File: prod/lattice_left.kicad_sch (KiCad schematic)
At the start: 84 parts, among them J1 USB_C_Receptacle, J2 USB_C_Receptacle, J3 Conn_01x05, SW1 SW_Push, SW2 SW_Push, U1 RP2040, U2 XC6206PxxxMR, U3 USBLC6-2SC6, U4 W25Q128JVS, Y1 12MHz

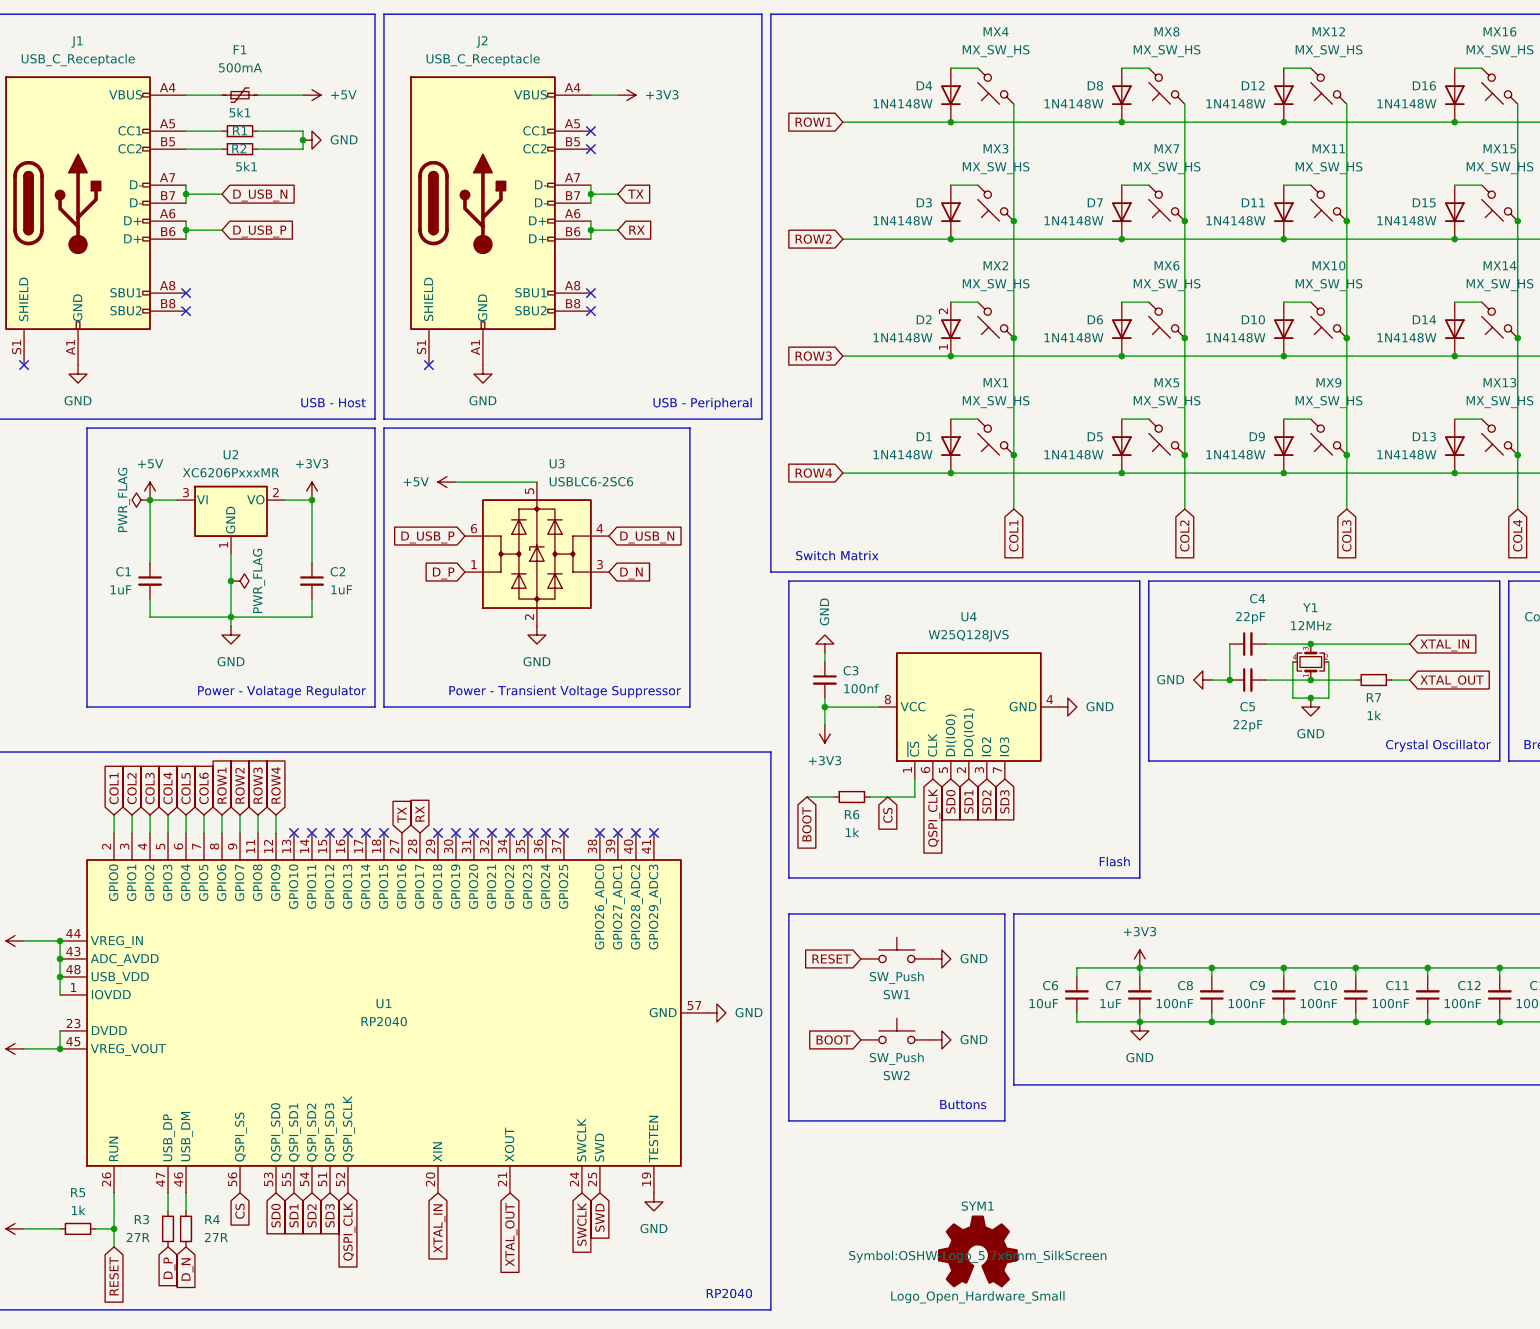
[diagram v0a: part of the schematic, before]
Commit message: component placement
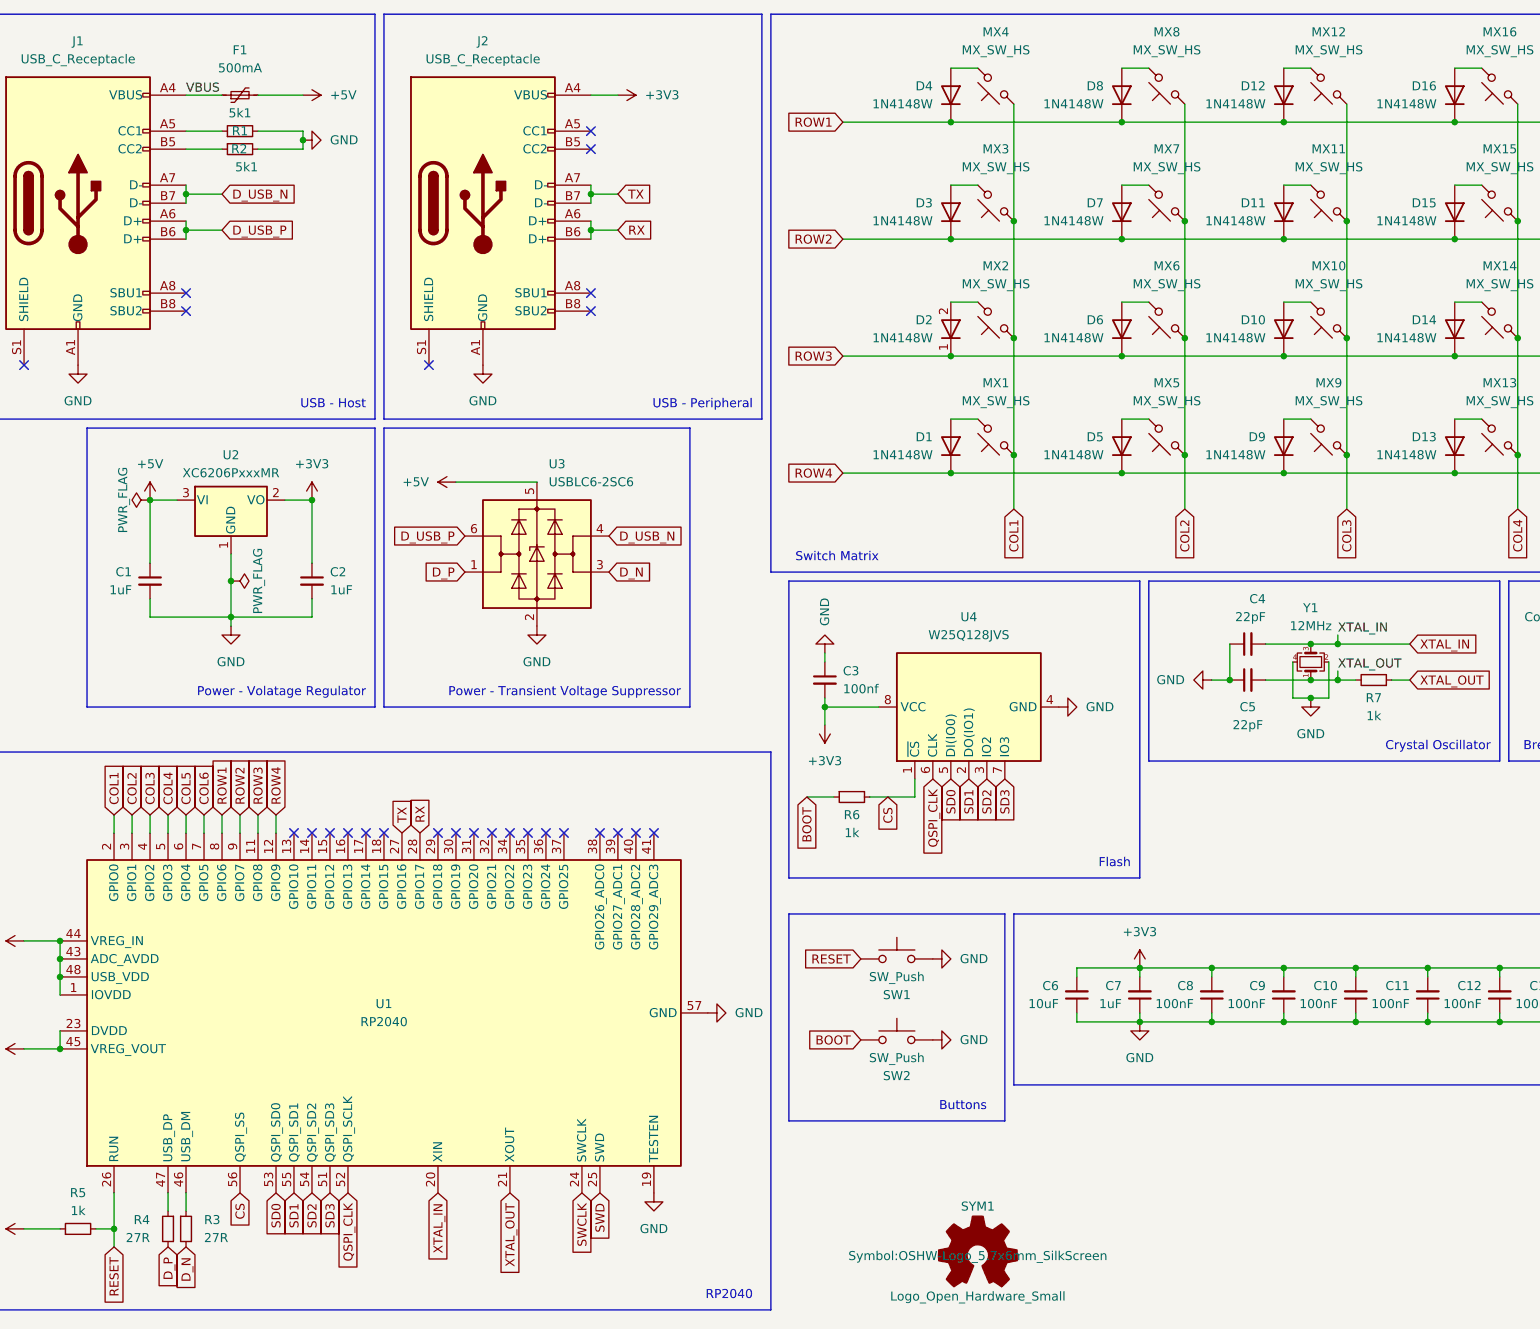
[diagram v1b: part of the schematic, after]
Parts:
- renumbered R4 to R3, R3 to R4
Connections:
- net XTAL_OUT: now also C5.2, R7.2, Y1.1
- net VBUS: now reaches F1.1, J1.A4 (VBUS), J1.A9 (VBUS), J1.B4 (VBUS), J1.B9 (VBUS)
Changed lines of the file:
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@@
   (junction (at 204.47 107.95) (diameter 0) (color 0 0 0 0)
   )
+  (junction (at 208.28 102.87) (diameter 0) (color 0 0 0 0)
+  )
   (junction (at 248.92 78.74) (diameter 0) (color 0 0 0 0)
   )
@@
   (junction (at 52.07 93.98) (diameter 0) (color 0 0 0 0)
   )
+  (junction (at 208.28 107.95) (diameter 0) (color 0 0 0 0)
+  )
   (junction (at 220.98 148.59) (diameter 0) (color 0 0 0 0)
   )
@@
     (stroke (width 0) (type default))
   )
+  (wire (pts (xy 208.28 101.6) (xy 208.28 102.87))
+    (stroke (width 0) (type default))
+  )
   (wire (pts (xy 186.69 26.67) (xy 186.69 43.18))
     (stroke (width 0) (type default))
@@
     (stroke (width 0) (type default))
   )
+  (wire (pts (xy 208.28 106.68) (xy 208.28 107.95))
+    (stroke (width 0) (type default))
+  )
   (wire (pts (xy 177.8 45.72) (xy 200.66 45.72))
     (stroke (width 0) (type default))
@@
     (stroke (width 0) (type default))
   )
-  (wire (pts (xy 204.47 107.95) (xy 210.82 107.95))
+  (wire (pts (xy 204.47 107.95) (xy 208.28 107.95))
     (stroke (width 0) (type default))
   )
@@
     (stroke (width 0) (type default))
   )
-  (wire (pts (xy 204.47 102.87) (xy 218.44 102.87))
+  (wire (pts (xy 204.47 102.87) (xy 208.28 102.87))
     (stroke (width 0) (type default))
   )
@@
     (stroke (width 0) (type default))
   )
+  (wire (pts (xy 208.28 102.87) (xy 218.44 102.87))
+    (stroke (width 0) (type default))
+  )
   (wire (pts (xy 241.3 148.59) (xy 241.3 149.86))
     (stroke (width 0) (type default))
@@
     (stroke (width 0) (type default))
   )
+  (wire (pts (xy 208.28 107.95) (xy 210.82 107.95))
+    (stroke (width 0) (type default))
+  )
   (wire (pts (xy 180.34 148.59) (xy 180.34 149.86))
     (stroke (width 0) (type default))
@@
     (effects (font (size 1.27 1.27)) (justify right bottom))
   )
+  (label "VBUS" (at 45.72 25.4 0) (fields_autoplaced)
+    (effects (font (size 1.27 1.27)) (justify left bottom))
+  )
+  (label "XTAL_IN" (at 208.28 101.6 0) (fields_autoplaced)
+    (effects (font (size 1.27 1.27)) (justify left bottom))
+  )
+  (label "XTAL_OUT" (at 208.28 106.68 0) (fields_autoplaced)
+    (effects (font (size 1.27 1.27)) (justify left bottom))
+  )
   (global_label "ROW1" (shape input) (at 138.43 29.21 180) (fields_autoplaced)
     (effects (font (size 1.27 1.27)) (justify right))
@@
     )
   )
-  (symbol (lib_id "Device:R_Small") (at 43.18 185.42 0) (unit 1)
-    (in_bom yes) (on_board yes) (dnp no) (fields_autoplaced)
-    (property "Reference" "R3" (at 40.64 184.15 0)
-      (effects (font (size 1.27 1.27)) (justify right))
+  (symbol (lib_id "Device:R_Small") (at 43.18 185.42 0) (mirror y) (unit 1)
+    (in_bom yes) (on_board yes) (dnp no)
+    (property "Reference" "R4" (at 40.64 184.15 0)
+      (effects (font (size 1.27 1.27)) (justify left))
     )
     (property "Value" "27R" (at 40.64 186.69 0)
-      (effects (font (size 1.27 1.27)) (justify right))
+      (effects (font (size 1.27 1.27)) (justify left))
     )
     (property "Footprint" "Resistor_SMD:R_0603_1608Metric" (at 43.18 185.42 0)
@@
       (project "lattice_left"
         (path "/7175bad1-6d67-4925-85bf-3e5286dbd285"
-          (reference "R3") (unit 1)
+          (reference "R4") (unit 1)
         )
       )
@@
   (symbol (lib_id "Device:R_Small") (at 45.72 185.42 0) (unit 1)
     (in_bom yes) (on_board yes) (dnp no) (fields_autoplaced)
-    (property "Reference" "R4" (at 48.26 184.15 0)
+    (property "Reference" "R3" (at 48.26 184.15 0)
       (effects (font (size 1.27 1.27)) (justify left))
     )
@@
       (project "lattice_left"
         (path "/7175bad1-6d67-4925-85bf-3e5286dbd285"
-          (reference "R4") (unit 1)
+          (reference "R3") (unit 1)
         )
       )

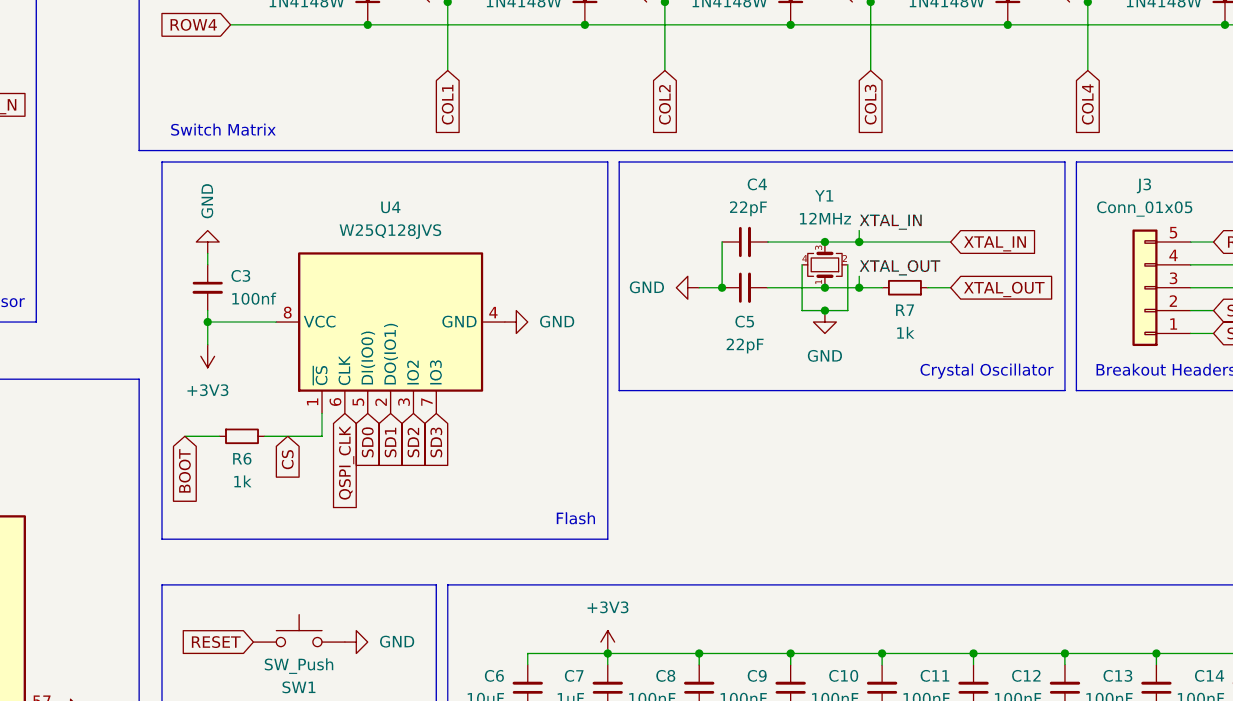
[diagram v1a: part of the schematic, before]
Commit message: component placement (swap crystal and flash)
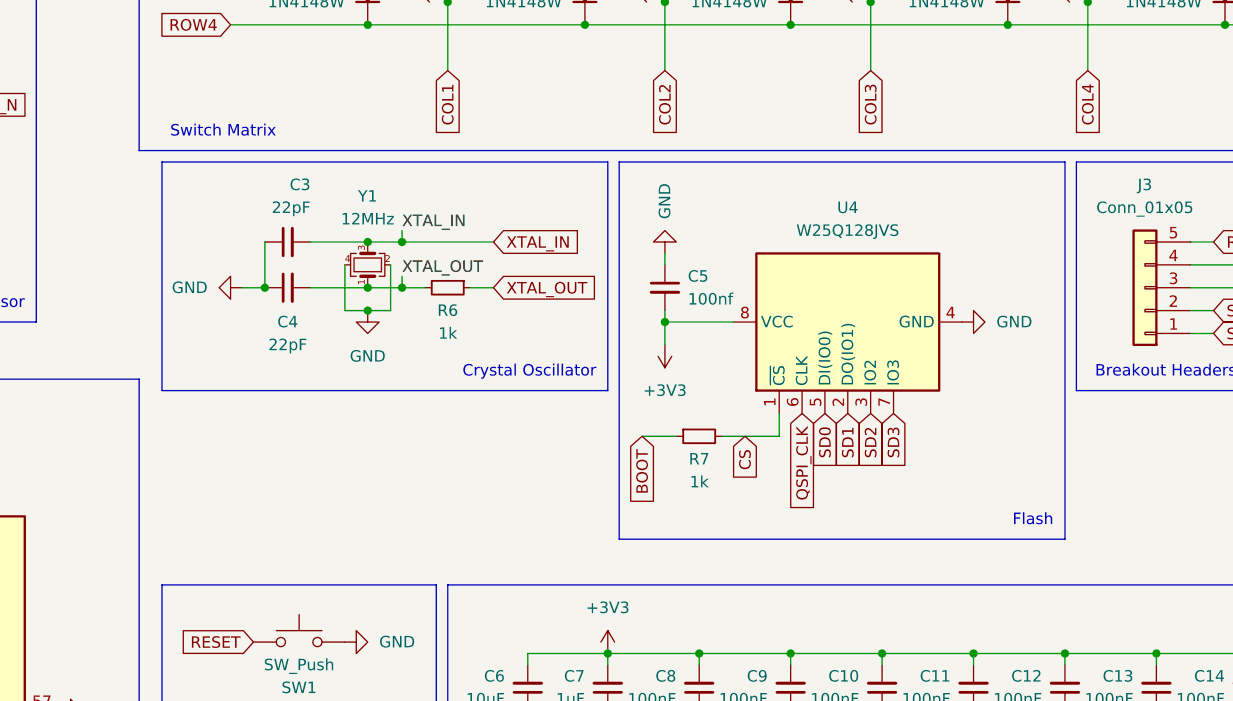
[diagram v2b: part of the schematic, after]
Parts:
- renumbered C4 to C3, C5 to C4, C3 to C5, R7 to R6, R6 to R7
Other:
- title: (none) -> lattice (left)
- moved on the sheet: C3, C4, C5, R6, R7, U4, Y1

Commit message: component placement
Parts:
- removed J3: Conn_01x05, lattice:PinHeader_1x05_P2.54mm_Vertical, symbol Connector_Generic:Conn_01x05
- C1, C10, C16, C2: footprint Capacitor_SMD:C_0603_1608Metric -> Capacitor_SMD:C_0402_1005Metric
- C11: renamed from C9; footprint Capacitor_SMD:C_0603_1608Metric -> Capacitor_SMD:C_0402_1005Metric
- C12: renamed from C8; footprint Capacitor_SMD:C_0603_1608Metric -> Capacitor_SMD:C_0402_1005Metric
- C13: renamed from C7; footprint Capacitor_SMD:C_0603_1608Metric -> Capacitor_SMD:C_0402_1005Metric
- C14: renamed from C6; footprint Capacitor_SMD:C_0603_1608Metric -> Capacitor_SMD:C_0402_1005Metric
- C15: renamed from C17; footprint Capacitor_SMD:C_0603_1608Metric -> Capacitor_SMD:C_0402_1005Metric
- C17: renamed from C15; footprint Capacitor_SMD:C_0603_1608Metric -> Capacitor_SMD:C_0402_1005Metric
- C3: renamed from C5; footprint Capacitor_SMD:C_0603_1608Metric -> Capacitor_SMD:C_0402_1005Metric
- C4: renamed from C3; footprint Capacitor_SMD:C_0603_1608Metric -> Capacitor_SMD:C_0402_1005Metric
- C5: renamed from C4; footprint Capacitor_SMD:C_0603_1608Metric -> Capacitor_SMD:C_0402_1005Metric
- C6: renamed from C14; footprint Capacitor_SMD:C_0603_1608Metric -> Capacitor_SMD:C_0402_1005Metric
- C7: renamed from C13; footprint Capacitor_SMD:C_0603_1608Metric -> Capacitor_SMD:C_0402_1005Metric
- C8: renamed from C12; footprint Capacitor_SMD:C_0603_1608Metric -> Capacitor_SMD:C_0402_1005Metric
- C9: renamed from C11; footprint Capacitor_SMD:C_0603_1608Metric -> Capacitor_SMD:C_0402_1005Metric
- F1: footprint Fuse:Fuse_0603_1608Metric -> Fuse:Fuse_0402_1005Metric
- R1, R2, R5: footprint Resistor_SMD:R_0603_1608Metric -> Resistor_SMD:R_0402_1005Metric
- R3: renamed from R7; footprint Resistor_SMD:R_0603_1608Metric -> Resistor_SMD:R_0402_1005Metric
- R4: renamed from R6; footprint Resistor_SMD:R_0603_1608Metric -> Resistor_SMD:R_0402_1005Metric
- R6: renamed from R4; footprint Resistor_SMD:R_0603_1608Metric -> Resistor_SMD:R_0402_1005Metric
- R7: renamed from R3; footprint Resistor_SMD:R_0603_1608Metric -> Resistor_SMD:R_0402_1005Metric
- renumbered D4 to D1, D11 to D10, D10 to D11, D9 to D12, D16 to D13, D15 to D14, D14 to D15, D13 to D16, D20 to D17, D19 to D18, D18 to D19, D3 to D2, D17 to D20, D24 to D21, D23 to D22, D22 to D23, D21 to D24, D2 to D3, D1 to D4, D8 to D5, D7 to D6, D6 to D7, D5 to D8, D12 to D9, MX4 to MX1, MX11 to MX10, MX10 to MX11, MX9 to MX12, MX16 to MX13, MX15 to MX14, MX14 to MX15, MX13 to MX16, MX20 to MX17, MX19 to MX18, MX18 to MX19, MX3 to MX2, MX17 to MX20, MX24 to MX21, MX23 to MX22, MX22 to MX23, MX21 to MX24, MX2 to MX3, MX1 to MX4, MX8 to MX5, MX7 to MX6, MX6 to MX7, MX5 to MX8, MX12 to MX9, U2 to U1, U3 to U2, U4 to U3, U1 to U4
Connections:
- net SWCLK: no longer names the net of U4.24 (SWCLK)
- net SWD: no longer names the net of U4.25 (SWD)
- no-connect marks 26 -> 28
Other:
- note removed: "Breakout Headers"
- moved on the sheet: C1, C10, C11, C12, C13, C14, C15, C16, C17, C2, C3, C4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
